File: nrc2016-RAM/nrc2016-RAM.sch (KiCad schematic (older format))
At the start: 3 parts, among them P1 CONN_01X40, U1 ATF16V8CV, U2 62256

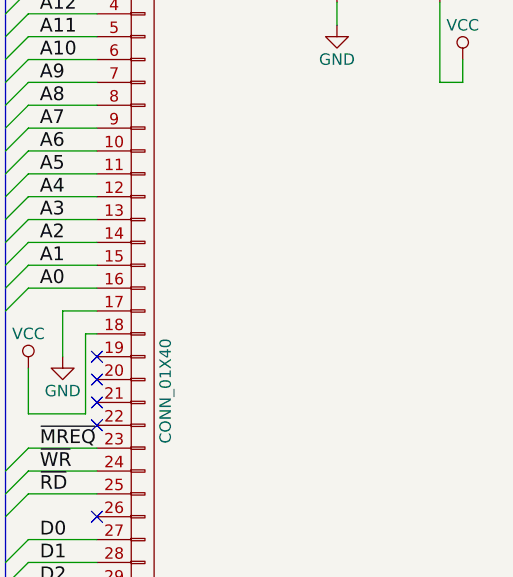
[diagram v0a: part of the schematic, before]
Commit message: Added decoupling caps to RAM board schematic
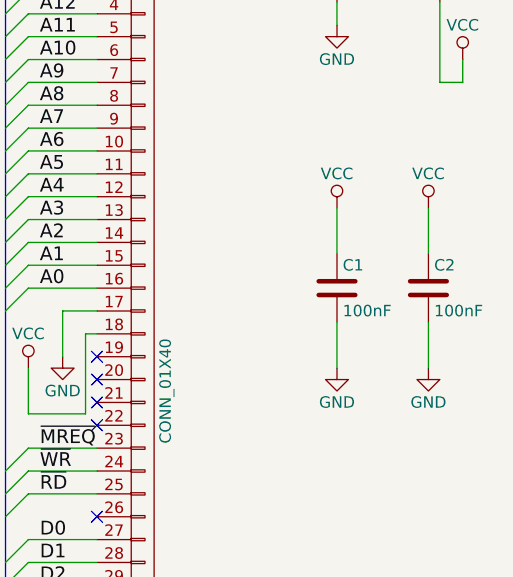
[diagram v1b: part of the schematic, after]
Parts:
- added C1, C2: 100nF, symbol C
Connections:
- net GND: now also C1.2, C2.2
- net VCC: now also C1.1, C2.1
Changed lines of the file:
@@
 Wire Wire Line
 	6350 3600 6600 3600
+$Comp
+L C C1
+U 1 1 57A49646
+P 7700 3050
+F 0 "C1" H 7725 3150 50  0000 L CNN
+F 1 "100nF" H 7725 2950 50  0000 L CNN
+F 2 "" H 7738 2900 50  0000 C CNN
+F 3 "" H 7700 3050 50  0000 C CNN
+	1    7700 3050
+	1    0    0    -1
+$EndComp
+$Comp
+L C C2
+U 1 1 57A4967D
+P 8100 3050
+F 0 "C2" H 8125 3150 50  0000 L CNN
+F 1 "100nF" H 8125 2950 50  0000 L CNN
+F 2 "" H 8138 2900 50  0000 C CNN
+F 3 "" H 8100 3050 50  0000 C CNN
+	1    8100 3050
+	1    0    0    -1
+$EndComp
+Wire Wire Line
+	7700 2900 7700 2700
+Wire Wire Line
+	8100 2900 8100 2700
+Wire Wire Line
+	7700 3200 7700 3400
+Wire Wire Line
+	8100 3200 8100 3400
+$Comp
+L GND #PWR?
+U 1 1 57A497E6
+P 7700 3400
+F 0 "#PWR?" H 7700 3150 50  0001 C CNN
+F 1 "GND" H 7700 3250 50  0000 C CNN
+F 2 "" H 7700 3400 50  0000 C CNN
+F 3 "" H 7700 3400 50  0000 C CNN
+	1    7700 3400
+	1    0    0    -1
+$EndComp
+$Comp
+L GND #PWR?
+U 1 1 57A49800
+P 8100 3400
+F 0 "#PWR?" H 8100 3150 50  0001 C CNN
+F 1 "GND" H 8100 3250 50  0000 C CNN
+F 2 "" H 8100 3400 50  0000 C CNN
+F 3 "" H 8100 3400 50  0000 C CNN
+	1    8100 3400
+	1    0    0    -1
+$EndComp
+$Comp
+L VCC #PWR?
+U 1 1 57A49833
+P 7700 2700
+F 0 "#PWR?" H 7700 2550 50  0001 C CNN
+F 1 "VCC" H 7700 2850 50  0000 C CNN
+F 2 "" H 7700 2700 50  0000 C CNN
+F 3 "" H 7700 2700 50  0000 C CNN
+	1    7700 2700
+	1    0    0    -1
+$EndComp
+$Comp
+L VCC #PWR?
+U 1 1 57A4984D
+P 8100 2700
+F 0 "#PWR?" H 8100 2550 50  0001 C CNN
+F 1 "VCC" H 8100 2850 50  0000 C CNN
+F 2 "" H 8100 2700 50  0000 C CNN
+F 3 "" H 8100 2700 50  0000 C CNN
+	1    8100 2700
+	1    0    0    -1
+$EndComp
 $EndSCHEMATC
